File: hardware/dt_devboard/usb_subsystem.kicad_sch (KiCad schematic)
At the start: 2 parts

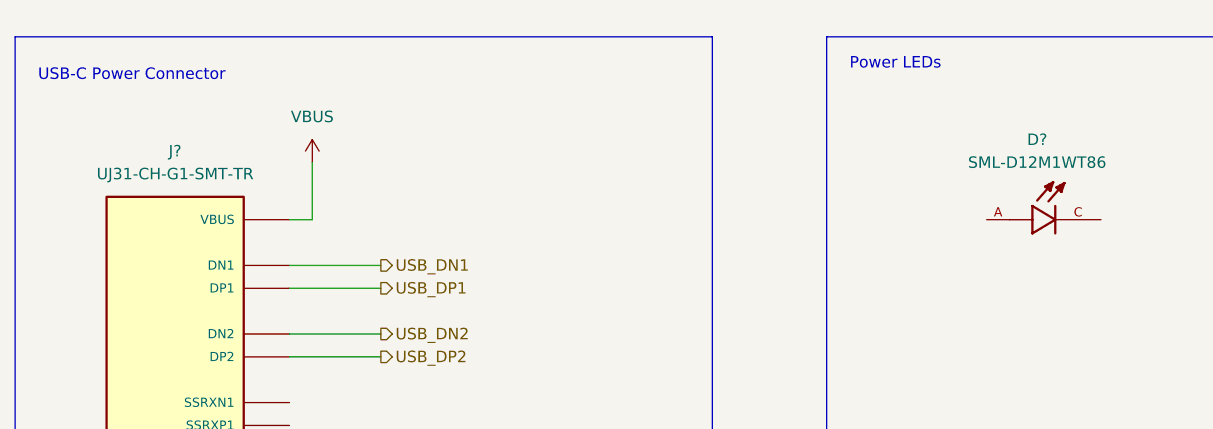
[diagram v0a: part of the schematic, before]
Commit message: added schematic sheets, symbols, and esp32 design
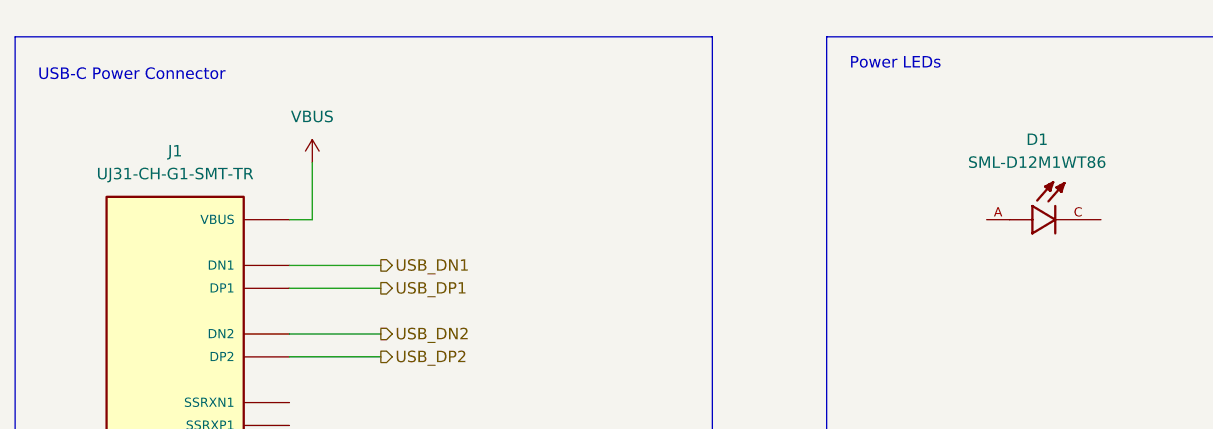
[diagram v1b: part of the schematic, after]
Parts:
- gave numbers to parts that had none: 2
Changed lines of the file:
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@@
   (symbol (lib_id "power:VBUS") (at 52.07 29.21 0) (unit 1)
     (in_bom yes) (on_board yes) (fields_autoplaced)
-    (property "Reference" "#PWR?" (id 0) (at 52.07 33.02 0)
+    (property "Reference" "#PWR024" (id 0) (at 52.07 33.02 0)
       (effects (font (size 1.27 1.27)) hide)
     )
@@
   (symbol (lib_id "UJ31-CH-G1-SMT-TR:UJ31-CH-G1-SMT-TR") (at 36.83 66.04 0) (unit 1)
     (in_bom yes) (on_board yes) (fields_autoplaced)
-    (property "Reference" "J?" (id 0) (at 36.83 27.94 0))
+    (property "Reference" "J1" (id 0) (at 36.83 27.94 0))
     (property "Value" "UJ31-CH-G1-SMT-TR" (id 1) (at 36.83 30.48 0))
     (property "Footprint" "CUI_UJ31-CH-G1-SMT-TR" (id 2) (at 36.83 66.04 0)
@@
   (symbol (lib_id "power:GND") (at 52.07 99.06 0) (unit 1)
     (in_bom yes) (on_board yes) (fields_autoplaced)
-    (property "Reference" "#PWR?" (id 0) (at 52.07 105.41 0)
+    (property "Reference" "#PWR025" (id 0) (at 52.07 105.41 0)
       (effects (font (size 1.27 1.27)) hide)
     )
@@
   (symbol (lib_id "SML-D12M1WT86:SML-D12M1WT86") (at 134.62 35.56 0) (unit 1)
     (in_bom yes) (on_board yes) (fields_autoplaced)
-    (property "Reference" "D?" (id 0) (at 132.6134 26.67 0))
+    (property "Reference" "D1" (id 0) (at 132.6134 26.67 0))
     (property "Value" "SML-D12M1WT86" (id 1) (at 132.6134 29.21 0))
     (property "Footprint" "LED_SML-D12M1WT86" (id 2) (at 134.62 35.56 0)
